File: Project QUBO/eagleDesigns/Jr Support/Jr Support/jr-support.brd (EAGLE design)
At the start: 242.6 x 96.8 mm, 209 parts, among them U1 PCA9685, U2 BME280

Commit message: 
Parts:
- removed 2PIN_3: KK254_VERT_2PIN22-29-2021, molex:KK254_VERT_2PIN
- removed 2PIN_7: Vin_OUT, molex:KK254_VERT_2PIN
- removed 2PIN_8: 12V_OUT, molex:KK254_VERT_2PIN
- removed 2PIN_9: 5V_OUT, molex:KK254_VERT_2PIN
- removed 4PIN_8: Depth Sensor, molex:KK254_VERT_4PIN
- removed 4PIN_9: CPU PWR, molex:KK254_VERT_4PIN
- removed U$1, U$24: LT8640, linear:QFN18-3X4
- removed U$21: (no value), texas:SM8
- removed U$41, U$55, U$56: INA219SOT23, texas:SOT-23-8
- removed U$42, U$43, U$44: ADC121C021, texas:VSSOP-8
- removed U$7: ADS7828, texas:TSSOP16
- removed U2: BME280, BME280ComponentLibrary:BME280_LGA
- added 12V_CURR_ADC, 5V_CURR_ADC, V-THRUST_CURR_ADC: ADC121C021, texas:VSSOP-8
- added 12V_OUT: 12V_OUT, molex:KK254_VERT_2PIN
- added 12V_REG, 5V_REG: LT8640, linear:QFN18-3X4
- added 12V_VOLTAGE, 5V_VOLTAGE, V-THRUST_VOLAGE: INA219SOT23, texas:SOT-23-8
- added 5V_OUT: 5V_OUT, molex:KK254_VERT_2PIN
- added BME280: BME280, BME280ComponentLibrary:BME280_LGA
- added CPU_ON: KK254_VERT_2PIN22-29-2021, molex:KK254_VERT_2PIN
- added CPU_PWR: CPU PWR, molex:KK254_VERT_4PIN
- added DEPTH_SENS: Depth Sensor, molex:KK254_VERT_4PIN
- added I2C_SHIFT: (no value), texas:SM8
- added THRUSTER_CURR_ADC: ADS7828, texas:TSSOP16
- added V-THRUST_OUT: Vin_OUT, molex:KK254_VERT_2PIN
- moved R2 301.7 mm to (146.7, 69.8), turned to 270 degrees
- moved C68 272.1 mm to (280.7, 48.9)
- moved U$65 272.1 mm to (285.8, 50.2)
- moved C54 262.4 mm to (119.4, 87.6)
- moved R13 260.1 mm to (101.0, 21.6)
- moved R28 260.1 mm to (106.7, 21.6)
- moved LED1 260.1 mm to (102.2, 26.7)
- moved U$58 260.1 mm to (100.3, 17.1)
- moved THRUST1 260.0 mm to (120.0, 92.1)
- moved C55 256.2 mm to (92.7, 49.5), turned to 180 degrees
- moved FAN2 255.0 mm to (267.3, 37.5), turned to 270 degrees
- moved C58 248.8 mm to (79.4, 49.5), turned to 180 degrees
- moved U$66 234.9 mm to (81.3, -33.7), turned to 90 degrees
- moved U$22 232.9 mm to (124.5, 49.5), turned to 180 degrees
- moved U$31 232.7 mm to (114.9, 87.6)
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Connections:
- removed net N$46: C42.1, C61.1, C62.P$1, L1.P$2, R23.2, U$2.P$1, U$2.P$2, U$24.1
- new net SW-5V: 5V_REG.1, C2.1, C42.1, C61.1, C62.P$1, L1.P$2, R23.2, U$2.P$1, U$2.P$2, U$2.P$8
- net 12V: now also 12V_OUT.P$1, CPU_PWR.P$3, CPU_PWR.P$4; no longer 2PIN_8.P$1, 4PIN_9.P$3, 4PIN_9.P$4
- net 3V3: now also BME280.P$2, BME280.P$5, BME280.P$6, BME280.P$8, I2C_SHIFT.P$2; no longer U$21.P$2, U2.P$2, U2.P$5, U2.P$6, U2.P$8
- net 5V: now also 12V_CURR_ADC.P$5, 5V_CURR_ADC.P$5, 5V_CURR_ADC.P$6, 5V_OUT.P$1, DEPTH_SENS.P$4, THRUSTER_CURR_ADC.10, THRUSTER_CURR_ADC.16, V-THRUST_CURR_ADC.P$3, V-THRUST_CURR_ADC.P$5, V-THRUST_CURR_ADC.P$6; no longer 2PIN_9.P$1, 4PIN_8.P$4, C2.1, U$2.P$8, U$42.P$5, U$42.P$6, U$43.P$3, U$43.P$5, U$43.P$6, U$44.P$5, U$7.10, U$7.16
- net CPU_ON: now also 12V_REG.14; no longer U$1.14
- net GND: now also 12V_CURR_ADC.P$3, 12V_CURR_ADC.P$6, 12V_CURR_ADC.P$7, 12V_OUT.P$2, 12V_REG.10, 12V_REG.11, 12V_REG.18, 12V_REG.6, 12V_REG.7, 12V_VOLTAGE.P$3, 12V_VOLTAGE.P$7, 5V_CURR_ADC.P$3, 5V_CURR_ADC.P$7, 5V_OUT.P$2, 5V_REG.10, 5V_REG.11, 5V_REG.18, 5V_REG.6, 5V_REG.7, 5V_VOLTAGE.P$3, 5V_VOLTAGE.P$7, 5V_VOLTAGE.P$8, BME280.P$1, BME280.P$7, CPU_PWR.P$1, CPU_PWR.P$2, DEPTH_SENS.P$3, I2C_SHIFT.P$1, THRUSTER_CURR_ADC.12, THRUSTER_CURR_ADC.13, THRUSTER_CURR_ADC.9, V-THRUST_CURR_ADC.P$7, V-THRUST_OUT.P$2, V-THRUST_VOLAGE.P$3; no longer 2PIN_7.P$2, 2PIN_8.P$2, 2PIN_9.P$2, 4PIN_8.P$3, 4PIN_9.P$1, 4PIN_9.P$2, U$1.10, U$1.11, U$1.18, U$1.6, U$1.7, U$21.P$1, U$24.10, U$24.11, U$24.18, U$24.6, U$24.7, U$41.P$3, U$42.P$3, U$42.P$7, U$43.P$7, U$44.P$3, U$44.P$6, U$44.P$7, U$55.P$3, U$55.P$7, U$55.P$8, U$56.P$3, U$56.P$7, U$7.12, U$7.13, U$7.9, U2.P$1, U2.P$7
- net N$1: now also 12V_REG.15; no longer U$1.15
- net N$23: now also THRUSTER_CURR_ADC.11; no longer U$7.11
- net N$32: now also 12V_REG.21, 12V_REG.22, 12V_REG.8, 12V_REG.9; no longer U$1.21, U$1.22, U$1.8, U$1.9
- net N$40: now also 5V_REG.21, 5V_REG.22, 5V_REG.8, 5V_REG.9; no longer U$24.21, U$24.22, U$24.8, U$24.9
- net N$41: now also I2C_SHIFT.P$7, I2C_SHIFT.P$8; no longer U$21.P$7, U$21.P$8
- net N$42: now also 5V_REG.20; no longer U$24.20
- net N$43: now also 5V_REG.3; no longer U$24.3
- net N$44: now also 12V_REG.20; no longer U$1.20
- net N$45: now also 12V_REG.3; no longer U$1.3
- net N$48: now also 5V_REG.2; no longer U$24.2
- net N$49: now also 12V_VOLTAGE.P$1, 12V_VOLTAGE.P$2; no longer U$56.P$1, U$56.P$2
- net N$51: now also CPU_ON.P$2; no longer 2PIN_3.P$2
- net N$53: now also V-THRUST_CURR_ADC.P$4; no longer U$43.P$4
- net N$54: now also 12V_REG.2; no longer U$1.2
- net N$57: now also 5V_CURR_ADC.P$4; no longer U$42.P$4
- net N$58: now also V-THRUST_VOLAGE.P$1, V-THRUST_VOLAGE.P$2; no longer U$41.P$1, U$41.P$2
- net N$60: now also 12V_CURR_ADC.P$4; no longer U$44.P$4
- net N$61: now also CPU_ON.P$1; no longer 2PIN_3.P$1
- net N$7: now also 12V_REG.1; no longer U$1.1
- net N$76: now also 5V_REG.19; no longer U$24.19
- net N$77: now also 5V_VOLTAGE.P$1, 5V_VOLTAGE.P$2; no longer U$55.P$1, U$55.P$2
- net N$8: now also 5V_REG.15; no longer U$24.15
- net N$80: now also 12V_REG.19; no longer U$1.19
- net RELAY_OUT: now also 12V_REG.13, 12V_REG.4, 12V_VOLTAGE.P$4, 12V_VOLTAGE.P$8, 5V_REG.13, 5V_REG.14, 5V_REG.4, 5V_VOLTAGE.P$4, V-THRUST_VOLAGE.P$4, V-THRUST_VOLAGE.P$7, V-THRUST_VOLAGE.P$8; no longer U$1.13, U$1.4, U$24.13, U$24.14, U$24.4, U$41.P$4, U$41.P$7, U$41.P$8, U$55.P$4, U$56.P$4, U$56.P$8
- net SCL-3V3: now also BME280.P$4, DEPTH_SENS.P$1, I2C_SHIFT.P$3; no longer 4PIN_8.P$1, U$21.P$3, U2.P$4
- net SCL1: now also 12V_CURR_ADC.P$1, 12V_VOLTAGE.P$5, 5V_CURR_ADC.P$1, 5V_VOLTAGE.P$5, I2C_SHIFT.P$6, THRUSTER_CURR_ADC.14, V-THRUST_CURR_ADC.P$1, V-THRUST_VOLAGE.P$5; no longer U$21.P$6, U$41.P$5, U$42.P$1, U$43.P$1, U$44.P$1, U$55.P$5, U$56.P$5, U$7.14
- net SDA-3V3: now also BME280.P$3, DEPTH_SENS.P$2, I2C_SHIFT.P$4; no longer 4PIN_8.P$2, U$21.P$4, U2.P$3
- net SDA1: now also 12V_CURR_ADC.P$8, 12V_VOLTAGE.P$6, 5V_CURR_ADC.P$8, 5V_VOLTAGE.P$6, I2C_SHIFT.P$5, THRUSTER_CURR_ADC.15, V-THRUST_CURR_ADC.P$8, V-THRUST_VOLAGE.P$6; no longer U$21.P$5, U$41.P$6, U$42.P$8, U$43.P$8, U$44.P$8, U$55.P$6, U$56.P$6, U$7.15
- net T1_CURR: now also THRUSTER_CURR_ADC.1; no longer U$7.1
- net T2_CURR: now also THRUSTER_CURR_ADC.2; no longer U$7.2
- net T3_CURR: now also THRUSTER_CURR_ADC.3; no longer U$7.3
- net T4_CURR: now also THRUSTER_CURR_ADC.4; no longer U$7.4
- net T5_CURR: now also THRUSTER_CURR_ADC.5; no longer U$7.5
- net T6_CURR: now also THRUSTER_CURR_ADC.6; no longer U$7.6
- net T7_CURR: now also THRUSTER_CURR_ADC.7; no longer U$7.7
- net T8_CURR: now also THRUSTER_CURR_ADC.8; no longer U$7.8
- net V_THRUST: now also V-THRUST_OUT.P$1; no longer 2PIN_7.P$1

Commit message: 
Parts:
- moved CPU_PWR 295.6 mm to (235.6, 8.26)
- moved R22 221.5 mm to (87.6, 74.3), flipped to the bottom
- moved R9 41.7 mm to (98.4, 74.3), flipped to the bottom, turned to 0 degrees
- moved C33 0.90 mm to (97.2, 61.0)
- moved C37 0.90 mm to (97.2, 57.1)
- moved C22 0.90 mm to (110.5, 61.0)
- moved C29 0.90 mm to (110.5, 57.1)
- moved C56 0.90 mm to (83.8, 61.0)
- moved C57 0.90 mm to (83.8, 57.1)
- moved C12 0.64 mm to (87.6, 80.0)
- moved C15 0.64 mm to (73.7, 80.0)
- moved C6 0.64 mm to (114.9, 80.0)
- moved C9 0.64 mm to (101.6, 80.0)
- moved U$23 0.64 mm to (104.1, 59.1)
- moved U$29 0.64 mm to (90.8, 59.1)
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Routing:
- net GND: track 0.00 -> 46.1 mm, vias 0 -> 24
- net 5V: track 0.00 -> 39.4 mm, vias 0 -> 8
- net T4_CURR: track 0.00 -> 20.6 mm, vias 0 -> 1
- net T3_CURR: track 0.00 -> 17.7 mm, vias 0 -> 1
- net N$18: track 0.00 -> 3.23 mm
- net N$12: track 0.00 -> 3.23 mm
- net N$13: track 0.00 -> 3.23 mm
- net N$38: track 0.00 -> 3.23 mm
- net N$28: track 0.00 -> 3.23 mm
- net N$25: track 0.00 -> 3.23 mm
- net N$31: track 0.00 -> 3.23 mm
- net N$21: track 0.00 -> 3.23 mm
- net T8_CURR: track 0.00 -> 2.54 mm, vias 0 -> 1
- net N$10: track 0.00 -> 2.53 mm
- added copper zone on layer 1, net 17
- added copper zone on layer 16, net 5V
- added copper zone on layer 16, net GND
- added copper zone on layer 1, net N$14
- added copper zone on layer 1, net N$15
- added copper zone on layer 1, net N$16
- added copper zone on layer 1, net N$19
- added copper zone on layer 1, net N$20
- added copper zone on layer 1, net N$22
- added copper zone on layer 1, net N$24
- added copper zone on layer 1, net N$26
- added copper zone on layer 1, net N$27
- added copper zone on layer 1, net N$29
- added copper zone on layer 1, net N$30
- added copper zone on layer 1, net N$36
- added copper zone on layer 1, net N$37
- added copper zone on layer 1, net N$39
- added copper zone on layer 1, net N$47
- added copper zone on layer 1, net V_THRUST

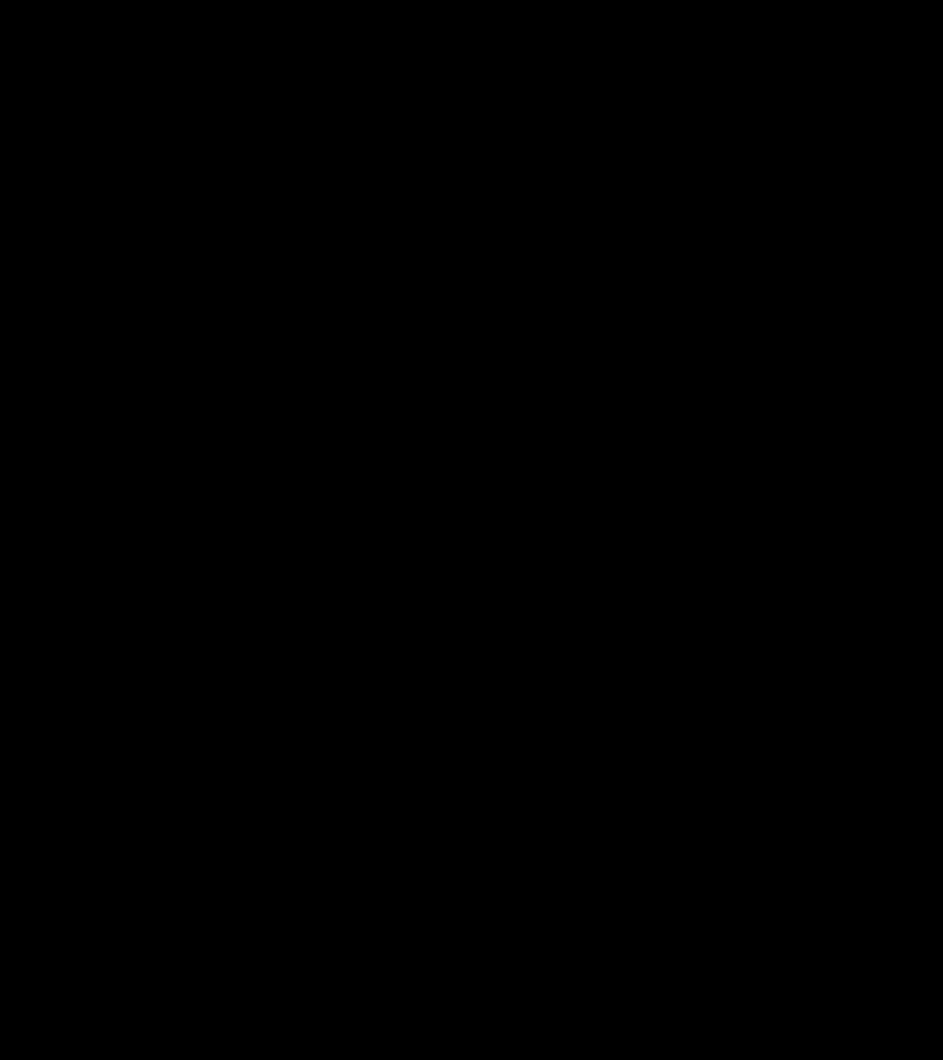
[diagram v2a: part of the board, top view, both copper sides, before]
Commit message: Main switch added to Jr Support.
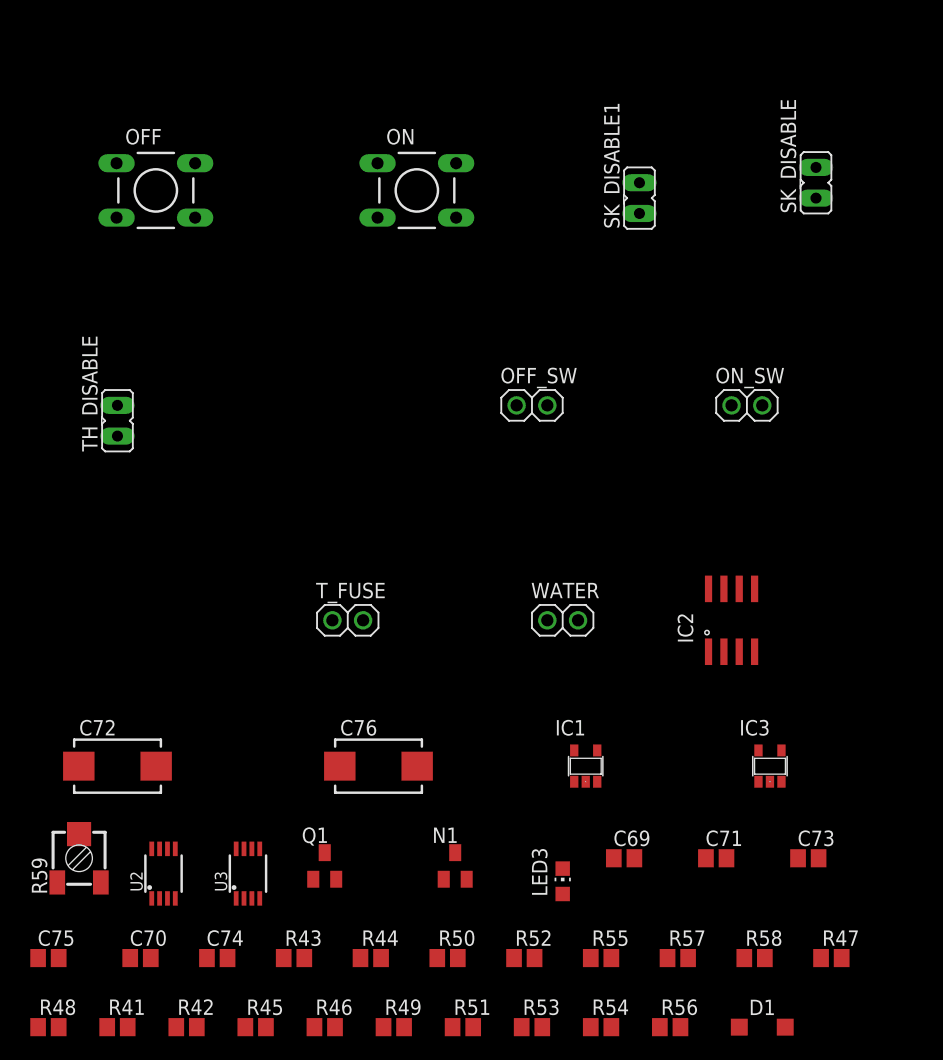
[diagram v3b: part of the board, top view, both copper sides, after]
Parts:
- added C69, C71, C73, C75: 100nF, resistor:C0805
- added C70, C74: 10nF, resistor:C0805
- added C72, C76: T491D475K050AT, resistor:CT7343
- added D1: MMSD4148, diode:SOD123
- added IC1, IC3: 74LVC1G08DBV, 74xx-little-us:SOT23-5
- added IC2: TLC2272D, texas:SO-08
- added LED3: Green, led:CHIP-LED0805
- added N1: 2N7002, transistor-fet:SOT23
- added OFF, ON: DTS-6, switch-tact:DTS-6
- added OFF_SW, ON_SW, T_FUSE, WATER: (no value), pinhead:1X02
- added Q1: FDN5618P, transistor-fet:SOT23
- added R41, R42, R45, R53, R54: 10k, resistor:R0805
- added R43: 845k, resistor:R0805
- added R44, R50: 115k, resistor:R0805
- added R46, R49, R51: 1M, resistor:R0805
- added R47, R48: 3.3k, resistor:R0805
- added R52, R55, R57, R58: 100k, resistor:R0805
- added R56: 470, resistor:R0805
- added R59: (no value), resistor:RTRIM3314J
- added SK_DISABLE, SK_DISABLE1, TH_DISABLE: (no value), jumper:JP1
- added U2, U3: LT3063, linear:MSOP8
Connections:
- new net +5V: C69.1, C71.1, IC2.8, IC3.5, R43.2, R55.1, R57.2, R59.3, SK_DISABLE.2, TH_DISABLE.2, T_FUSE.1, U2.3, U2.4
- new net FAULT: IC1.4, IC3.2, OFF.3, OFF.4, OFF_SW.1
- new net FET: IC3.4, N1.1, R53.2
- new net N$46: Q1.1, R41.1, R42.1
- new net N$81: D1.A, N1.3, R42.2
- new net N$82: R43.1, R44.2, U2.2
- new net N$83: C70.1, U2.1
- new net N$84: LED3.A, R47.1, R48.1
- new net N$85: R49.1, R50.2, U3.2
- new net N$86: C74.1, U3.1
- new net N$87: IC1.2, R51.2, TH_DISABLE.1, T_FUSE.2
- new net N$88: IC2.2, IC2.7, R52.1
- new net N$89: IC2.6, R52.2, R54.1
- new net N$90: IC2.5, R57.1, R58.2
- new net N$91: R54.2, R55.2, R56.1
- new net N$92: R56.2, WATER.1
- new net N$93: IC2.3, R59.2
- new net N$94: IC2.1, SK_DISABLE1.1
- new net ON_SW: D1.C, ON.3, ON.4, ON_SW.1
- new net SK: C73.1, IC3.1, R45.1, R46.2, SK_DISABLE.1
- new net SOFT_KILL: R45.2
- new net VCC: IC1.5
- new net VDD: C72.+, C76.+, Q1.3, R47.2, R48.2, U2.5, U2.6, U2.7, U3.5, U3.6, U3.7
- new net WATER: IC1.1, SK_DISABLE1.2
- net GND: now also C69.2, C70.2, C71.2, C72.-, C73.2, C74.2, C75.2, C76.-, IC1.3, IC2.4, IC3.3, LED3.C, N1.2, OFF.1, OFF.2, OFF_SW.2, ON.1, ON.2, ON_SW.2, R44.1, R46.1, R50.1, R51.1, R53.1, R58.1, R59.1, U2.8, U3.8, WATER.2
- net RELAY-BATT: now also Q1.2, R41.2
- net RELAY-CTRL: now also C75.1, R49.2, U3.3, U3.4

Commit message: 
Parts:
- R10, R11: value 10k -> 4.2k
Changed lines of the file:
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@@
 <element name="3V3_LED" library="led" package="0805" value="" x="-64.77" y="168.91"/>
 <element name="R1" library="resistor" package="R0805" value="10k" x="-138.43" y="152.4"/>
-<element name="R10" library="resistor" package="R0805" value="10k" x="-91.44" y="146.05"/>
-<element name="R11" library="resistor" package="R0805" value="10k" x="-96.52" y="146.05"/>
+<element name="R10" library="resistor" package="R0805" value="4.2k" x="-91.44" y="146.05"/>
+<element name="R11" library="resistor" package="R0805" value="4.2k" x="-96.52" y="146.05"/>
 <element name="R12" library="resistor" package="R0805" value="200k" x="-43.18" y="139.7"/>
 <element name="R14" library="resistor" package="R0805" value="41.2k" x="55.245" y="14.605" rot="R180"/>

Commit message: 
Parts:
- moved 12V_OUT 311.5 mm to (204.6, 6.35), turned to 180 degrees
- moved C51 298.6 mm to (162.8, 57.9), turned to 180 degrees
- moved 5V_OUT 298.2 mm to (162.8, 62.2)
- moved U$34 285.3 mm to (150.1, 85.9)
- moved C48 275.9 mm to (153.7, 57.9), turned to 180 degrees
- moved U$33 270.9 mm to (141.5, 85.9)
- moved C49 268.7 mm to (150.1, 83.6), turned to 180 degrees
- moved C43 265.1 mm to (162.1, 46.2), turned to 180 degrees
- moved V-THRUST_OUT 263.2 mm to (150.1, 79.0)
- moved U$32 255.7 mm to (132.1, 85.9)
- moved CAMERA1 252.6 mm to (132.3, 79.0)
- moved C47 250.8 mm to (141.5, 83.3)
- moved CAMERA2 248.8 mm to (141.2, 79.0)
- moved ETHERNET 238.2 mm to (153.4, 62.2)
- moved C46 237.2 mm to (132.1, 83.3), turned to 180 degrees
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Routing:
- net N$3: track 0.00 -> 53.5 mm, vias 0 -> 1
- net N$4: track 0.00 -> 49.6 mm, vias 0 -> 1
- net N$5: track 0.00 -> 45.3 mm, vias 0 -> 1
- net N$6: track 0.00 -> 37.6 mm, vias 0 -> 1
- net N$9: track 0.00 -> 33.2 mm, vias 0 -> 1
- net 5V: track 39.4 -> 52.6 mm, vias 8 -> 9

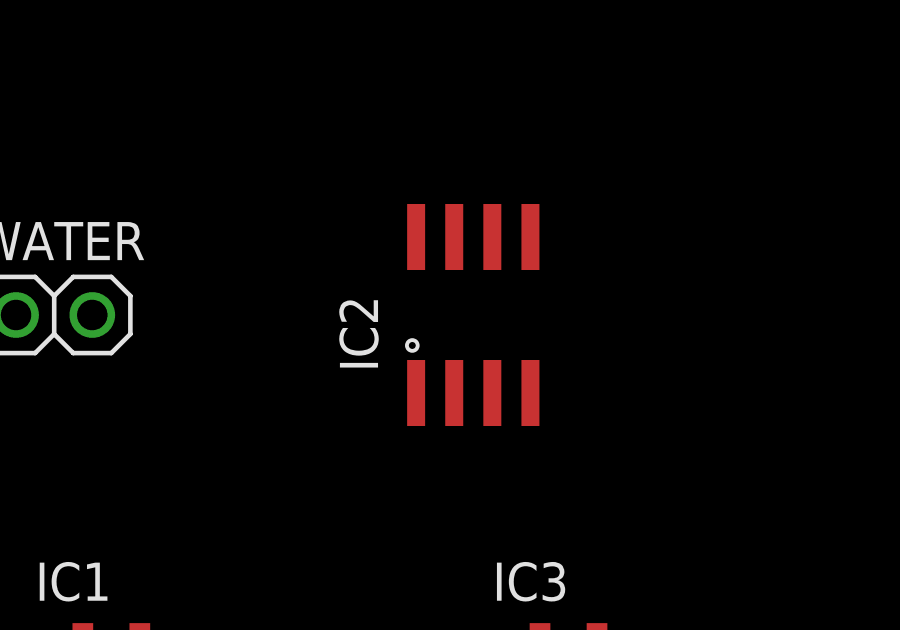
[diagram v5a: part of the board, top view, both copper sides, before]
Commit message: 
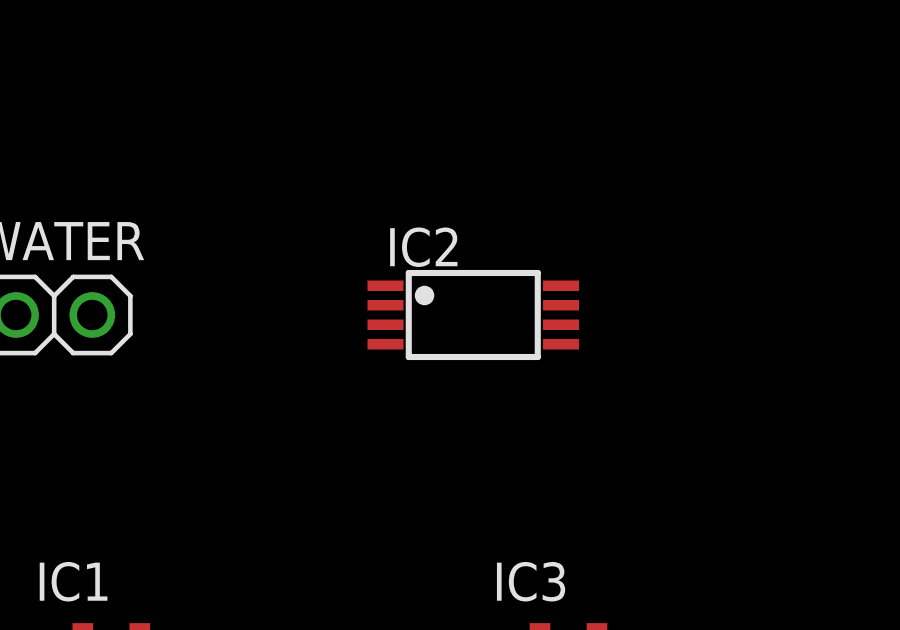
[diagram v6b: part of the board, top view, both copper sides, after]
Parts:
- IC2: value TLC2272D -> TLC2272PW; device texas:SO-08 -> texas:TSSOP8
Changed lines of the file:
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@@
 <element name="TH_DISABLE" library="jumper" package="JP1" value="" x="-137.16" y="-71.755"/>
 <element name="T_FUSE" library="pinhead" package="1X02" value="" x="-118.11" y="-88.265"/>
-<element name="IC2" library="texas" package="SO-08" value="TLC2272D" x="-86.36" y="-88.265"/>
+<element name="IC2" library="texas" package="TSSOP8" value="TLC2272PW" x="-86.36" y="-88.265"/>
 <element name="R52" library="resistor" package="R0805" value="100k" x="-103.505" y="-116.205"/>
 <element name="R53" library="resistor" package="R0805" value="10k" x="-102.87" y="-121.92"/>
@@
 <wire x1="-85.305" y1="-116.205" x2="-86.78" y2="-107.95" width="0" layer="19" extent="1-1"/>
 <wire x1="-118.77" y1="-100.33" x2="-127.34" y2="-107.17" width="0" layer="19" extent="1-1"/>
-<wire x1="-84.455" y1="-90.865" x2="-82.235" y2="-101.62" width="0" layer="19" extent="1-1"/>
+<wire x1="-89.285" y1="-89.24" x2="-82.235" y2="-101.62" width="0" layer="19" extent="1-1"/>
 <wire x1="-99.06" y1="-88.265" x2="-97.475" y2="-101.62" width="0" layer="19" extent="1-1"/>
 <wire x1="-101.6" y1="-70.485" x2="-99.06" y2="-88.265" width="0" layer="19" extent="1-1"/>
@@
 <wire x1="-96.1" y1="-107.95" x2="-88.48" y2="-107.95" width="0" layer="19" extent="1-1"/>
 <wire x1="-84.135" y1="-99.03" x2="-88.48" y2="-107.95" width="0" layer="19" extent="1-1"/>
-<wire x1="-88.265" y1="-85.665" x2="-84.135" y2="-99.03" width="0" layer="19" extent="1-1"/>
+<wire x1="-83.435" y1="-87.29" x2="-84.135" y2="-99.03" width="0" layer="19" extent="1-1"/>
 <wire x1="-119.38" y1="-88.265" x2="-132.375" y2="-111.27" width="0" layer="19" extent="1-1"/>
 <wire x1="-137.16" y1="-70.485" x2="-119.38" y2="-88.265" width="0" layer="19" extent="1-1"/>
-<wire x1="-79.375" y1="-50.8" x2="-88.265" y2="-85.665" width="0" layer="19" extent="1-1"/>
+<wire x1="-79.375" y1="-50.8" x2="-83.435" y2="-87.29" width="0" layer="19" extent="1-1"/>
 </signal>
 <signal name="VDD">
@@
 <contactref element="R52" pad="1"/>
 <contactref element="IC2" pad="2"/>
-<wire x1="-86.995" y1="-90.865" x2="-104.355" y2="-116.205" width="0" layer="19" extent="1-1"/>
-<wire x1="-86.995" y1="-85.665" x2="-86.995" y2="-90.865" width="0" layer="19" extent="1-1"/>
+<wire x1="-89.285" y1="-87.94" x2="-104.355" y2="-116.205" width="0" layer="19" extent="1-1"/>
+<wire x1="-83.435" y1="-87.94" x2="-89.285" y2="-87.94" width="0" layer="19" extent="1-1"/>
 </signal>
 <signal name="N$89">
@@
 <contactref element="R54" pad="1"/>
 <wire x1="-102.655" y1="-116.205" x2="-98.005" y2="-121.92" width="0" layer="19" extent="1-1"/>
-<wire x1="-85.725" y1="-85.665" x2="-102.655" y2="-116.205" width="0" layer="19" extent="1-1"/>
+<wire x1="-83.435" y1="-88.59" x2="-102.655" y2="-116.205" width="0" layer="19" extent="1-1"/>
 </signal>
 <signal name="N$90">
@@
 <contactref element="IC2" pad="5"/>
 <wire x1="-83.605" y1="-116.205" x2="-91.655" y2="-116.205" width="0" layer="19" extent="1-1"/>
-<wire x1="-84.455" y1="-85.665" x2="-83.605" y2="-116.205" width="0" layer="19" extent="1-1"/>
+<wire x1="-83.435" y1="-89.24" x2="-83.605" y2="-116.205" width="0" layer="19" extent="1-1"/>
 </signal>
 <signal name="N$91">
@@
 <contactref element="IC2" pad="3"/>
 <contactref element="R59" pad="2"/>
-<wire x1="-85.725" y1="-90.865" x2="-140.335" y2="-105.95" width="0" layer="19" extent="1-1"/>
+<wire x1="-89.285" y1="-88.59" x2="-140.335" y2="-105.95" width="0" layer="19" extent="1-1"/>
 </signal>
 <signal name="N$94">
 <contactref element="IC2" pad="1"/>
 <contactref element="SK_DISABLE1" pad="1"/>
-<wire x1="-93.98" y1="-54.61" x2="-88.265" y2="-90.865" width="0" layer="19" extent="1-1"/>
+<wire x1="-93.98" y1="-54.61" x2="-89.285" y2="-87.29" width="0" layer="19" extent="1-1"/>
 </signal>
 </signals>
